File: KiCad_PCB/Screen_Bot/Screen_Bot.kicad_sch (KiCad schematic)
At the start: 3 parts, among them U1 Adafruit TPS61023(5V), U2 Adafruit MPM3610 (3.3V)

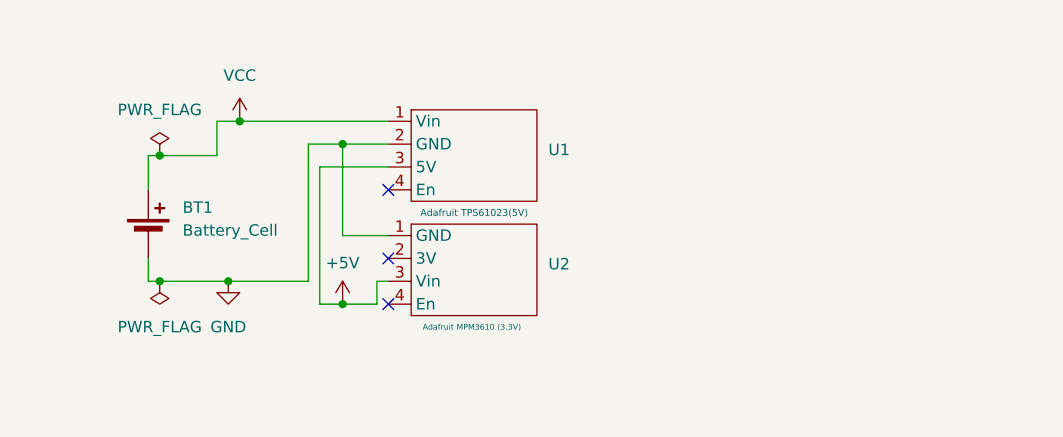
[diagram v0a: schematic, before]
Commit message: Update KiCad schematic and symbols
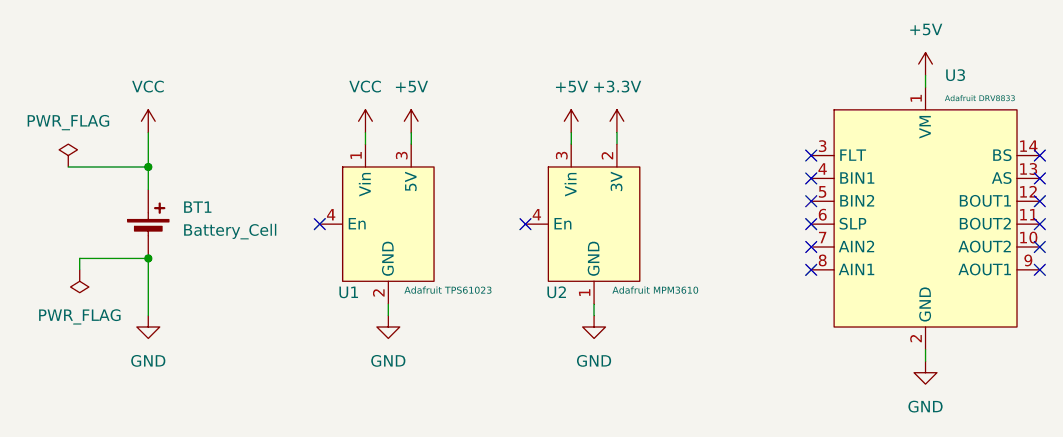
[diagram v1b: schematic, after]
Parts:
- added U3: Adafruit DRV8833, Screen_Bot:Adafruit_DRV8833, symbol Screen_Bot:Adafruit_DRV8833
- U1: value Adafruit TPS61023(5V) -> Adafruit TPS61023
- U2: value Adafruit MPM3610 (3.3V) -> Adafruit MPM3610
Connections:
- net +5V: now also U3.1 (VM)
- net GND: now also U3.2 (GND)
- net +3.3V: now reaches U2.2 (3V)
- no-connect marks 3 -> 14
